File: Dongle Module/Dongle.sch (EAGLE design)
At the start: 74 parts, among them Q2 2.5A/30V, U1 RFM69HCW, U10 74AHC1G125, U2 HALL-EFFECTSMD, U3 HALL-EFFECTSMD, U4 HALL-EFFECTSMD, U5 HALL-EFFECTSMD, U6 BQ27441-G1, U7 BQ24075, U8 ATSAMD21G-A, U9 3.3V, Y1 32.768kHz

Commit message: Worked on the laser and dongle schematics Placed the parts on the laser and dongle boards in their rough locations
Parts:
- removed C10: 1.0uF, SparkFun-Capacitors:1.0UF50V10%(1206)
- removed C11, C9: 10uF, SparkFun-Capacitors:10UF10V10%(0805)
- removed C3, C4, C5, C6: 0.1uF, SparkFun-Capacitors:0.1UF-25V(+80/-20%)(0603)
- removed C7: 1.0uF, SparkFun-Capacitors:1.0UF-16V-10%(0603)
- removed C8: 0.47uF, SparkFun-Capacitors:CAP0603-CAP
- removed D1: BLU, SparkFun-LED:LED-BLUE0603
- removed D2, D6: RED, SparkFun-LED:LED-RED0603
- removed D3: GREEN, SparkFun-LED:LED-GREEN0603
- removed D4: WHT, SparkFun-LED:LED-WHITE0603
- removed D5: BLUE, SparkFun-LED:LED-BLUE0603
- removed JP10: (no value), SparkFun-Connectors:JST_2MM_MALE
- removed JP11: (no value), mike-temp:M021X02_NO_SILK
- removed L1: FB - 30Ohm, SparkFun-Passives:INDUCTOR0603
- removed R11: 0.01, SparkFun-Resistors:RESISTOR1206
- removed R12: 1.1k, SparkFun-Passives:RESISTOR0603-RES
- removed R13, R14: 4.7K, SparkFun-Resistors:4.7KOHM-1/10W-1%(0603)
- removed R15, R2, R3, R4: 180, SparkFun-Resistors:180OHM1/10W1%(0603)
- removed R16: 1K, SparkFun-Resistors:1KOHM-1/10W-1%(0603)
- removed R17, R24: 100k, SparkFun-Resistors:100KOHM-1/10W-1%(0603)
- removed R18, R19, R22, R26: 10K, SparkFun-Resistors:10KOHM-1/10W-1%(0603)0603
- removed R5, R6, R7, R8, R9: 10K, SparkFun-Resistors:10KOHM1/10W1%(0603)0603
- removed S2: (no value), SparkFun-Electromechanical:SWITCH-SPDT-SMD-A
- removed S4: RESET, samd21-temp:SWITCH-MOMENTARY-2SMD-4.6X2.8MM
- removed SJ6: PWR-LED, SparkFun-Passives:JUMPER-PAD-2-NC_BY_TRACENO_SILK
- removed U2, U3, U4, U5: HALL-EFFECTSMD, SparkFun-Sensors:HALL-EFFECTSMD
- removed U6: BQ27441-G1, battery-management-temp:BQ27441-G1
- removed U7: BQ24075, battery-management-temp:BQ24075
- added ANT: (no value), SparkFun-Connectors:M01PTH_2MM
- added U$1: APA102, SAUVE:APA102
- JP22: value CORTEX_DEBUGPTH -> CORTEX_DEBUGSMD; device samd21-temp:CORTEX_DEBUGPTH -> SparkFun-Connectors:CORTEX_DEBUGSMD
- R1: value 180 -> 330; device SparkFun-Resistors:180OHM1/10W1%(0603) -> SparkFun-Resistors:330OHM1/10W1%(0603)
- S1: value SWITCH-MOMENTARY-2SMD-2 -> SWITCH-MOMENTARY-2SMD-4; device SparkFun-Electromechanical:SWITCH-MOMENTARY-2SMD-2 -> SparkFun-Electromechanical:SWITCH-MOMENTARY-2SMD-4
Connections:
- removed net !CE!: R17.1, U7.!CE!
- removed net !CHG!: R15.2, U7.!CHG!
- removed net !PGOOD!: R16.2, U7.!PGOOD!
- removed net 1.8V: C8.1, U6.VDD
- removed net A0: U8.PA02(AIN0/DAC)
- removed net A1: U8.PB08(AIN2/SER4:0/TC4:0)
- removed net A2: U8.PB09(AIN3/SER4:1/TC4:1)
- removed net A3: U8.PA04(AIN4/REFB/SER0:0/TC0:0)
- removed net AREF: U8.PA03(AIN1/REFA)
- removed net BATTERY_IN: C7.1, JP10.+, R11.2, U6.BAT, U6.SRP
- removed net BLU_PWM: R4.1
- removed net BMS_SCL: R14.1, U6.SCL
- removed net BMS_SDA: R13.1, U6.SDA
- removed net D0/RXI: U8.PA11(AIN19/SER0:3+)
- removed net D1/TXO: U8.PA10(AIN18/SER0:2+)
- removed net D10/SS: U8.PA18(SER1:2+)
- removed net D11/MOSI: U8.PA16(I2C/SER1:0+)
- removed net D12/MISO: U8.PA19(SER1:3+)
- removed net D13/SCK: U8.PA17(I2C/SER1:1+)
- removed net D2: U8.PA14(XIN/SER2:2+)
- removed net D3: U8.PA09(I2C/AIN17/SER0:1+)
- removed net D4: U8.PA08(I2C/AIN16/SER0:0+)
- removed net D5: U8.PA15(XOUT/SER2:3+)
- removed net D6: U8.PA20(SER5:2+)
- removed net D7: U8.PA21(SER5:3+)
- removed net D8: U8.PA06(AIN6/SER0:2/TC1:0)
- removed net D9: U8.PA07(AIN7/SER0:3/TC1:1)
- removed net EN1: R18.2, U7.EN1
- removed net EN2: U7.EN2
- removed net GPOUT: R26.1, U6.GPOUT
- removed net GRN_PWM: R2.1
- removed net HALL_DWN: R7.2, U3.OUT
- removed net HALL_LFT: R8.2, U4.OUT
- removed net HALL_RHT: R9.2, U5.OUT
- removed net HALL_UP: R6.2, U2.OUT
- removed net ILIM: R12.1, U7.ILIM
- removed net N$1: D3.A, R2.2
- removed net N$11: D5.C, R15.1
- removed net N$12: D6.C, R16.1
- removed net N$2: D2.A, R3.2
- removed net N$23: D7.C, SJ6.2
- removed net N$3: D1.A, R4.2
- removed net N$4: D4.A, R1.2
- removed net N$5: R24.2, S2.O
- removed net OUT: C9.1, D5.A, D6.A, R13.2, R14.2, R18.1, R19.1, R26.2, U7.OUT
- removed net RED_PWM: R3.1
- removed net RF_NSS: U1.NSS
- removed net RX_LED: U8.PB03(AIN11/SER5:1)
- removed net SCL: U8.PA23(I2C/SER3:0+)
- removed net SDA: U8.PA22(I2C/SER3:0+)
- removed net SYSOFF: S2.P, U7.SYSOFF
- removed net TRK_BTN: R5.2, S1.2
- removed net TS: R22.2, U6.BIN, U7.TS
- removed net TX_LED: U8.PA27
- removed net VCC: C3.1, C4.1, C5.1, C6.1, R5.1, R6.1, R7.1, R8.1, R9.1, U2.VCC, U3.VCC, U4.VCC, U5.VCC
- removed net V_BATT: C11.1, R11.1, R24.1, U6.SRN, U7.BAT
- removed net WHT_PWM: R1.1
- new net APA_CLK: U$1.CKI, U8.PA09(I2C/AIN17/SER0:1+)
- new net APA_MOSI: U$1.SDI, U8.PA08(I2C/AIN16/SER0:0+)
- new net RF_SS: U1.NSS, U8.PA18(SER1:2+)
- new net SEL_BTN: R1.2, S1.1, U8.PA15(XOUT/SER2:3+)
- net !RESET: no longer S4.2
- net 3.3V: now also S1.2, U$1.VCC; no longer L1.1
- net ANT: now also ANT.1
- net GND: now also D7.C, R1.1, U$1.GND; no longer C10.2, C11.2, C3.2, C4.2, C5.2, C6.2, C7.2, C8.2, C9.2, D1.C, D2.C, D3.C, D4.C, JP10.-, JP11.2, R12.2, R17.2, R19.2, R22.1, S1.1, S2.S, S4.1, SJ6.1, U2.GND, U3.GND, U4.GND, U5.GND, U6.PWPD, U6.VSS, U7.EP, U7.TMR, U7.VSS
- net RF_MISO: now also U8.PA19(SER1:3+)
- net RF_MOSI: now also U8.PA16(I2C/SER1:0+)
- net RF_SCK: now also U8.PA17(I2C/SER1:1+)
- net VDDANA: no longer L1.2
- net V_USB: no longer C10.1, JP11.1, U7.IN
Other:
- note removed: "BQ24075 - 1.5A USB-Friendly LiPo Battery Charger & Power-Path Management"
- note removed: "BQ27441-G1 Fuel Gauge"
- note removed: "Battery Charger/Monitor"
- note removed: "Battery Input"
- note removed: "Battery Range: 3.3-4.2V"
- note removed: "Charge Current Select"
- note removed: "I2C ADDR: 0x55"
- note removed: "I2C Pull-Ups"
- note removed: "PA12 is SPI MISO (on SPI header)."
- note removed: "PA13 is DGI GPIO0 (goes to EDBG)."
- note removed: "PA5 is A4"
- note removed: "PB2 is A5"
- note removed: "SYSOFF controls supply to the V_OUT pin. SYSOFF is active-high HIGH=OFF LOW=ON"
- note removed: "Shutoff Switch"
- note removed: "Supply Input"
- note removed: "Supply range: 4.35-6.4V"
- note removed: "TRACKBALL"
- note removed: "VCC Range: 2.5V - 5.25V"
- note removed: "VDD is 1.8V generated internally"
- moved on the sheet: C1, C12, C13, C14, C15, C16, C17, C18, C19, C2, D7, F1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

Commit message: Created, placed, and routed a starter board for the Camera Module
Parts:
- ANT: device SparkFun-Connectors:M01PTH_2MM -> SparkFun-Connectors:M01PTH_NO_SILK_YES_STOP
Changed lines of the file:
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@@
 <part name="GND5" library="SparkFun-Aesthetics" deviceset="GND" device=""/>
 <part name="SUPPLY5" library="SparkFun-Aesthetics" deviceset="3.3V" device=""/>
-<part name="ANT" library="SparkFun-Connectors" deviceset="M01" device="PTH_2MM"/>
+<part name="ANT" library="SparkFun-Connectors" deviceset="M01" device="PTH_NO_SILK_YES_STOP"/>
 </parts>
 <sheets>

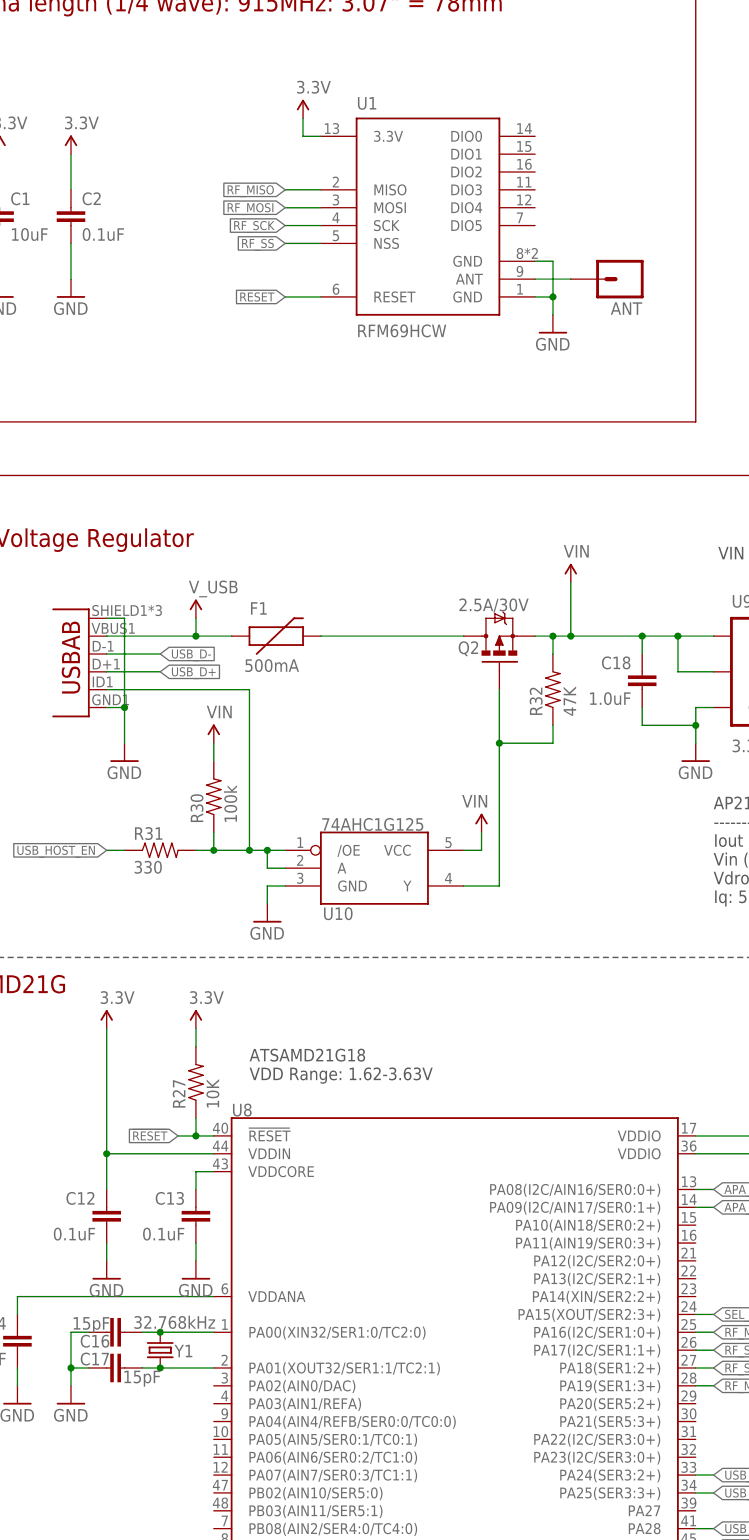
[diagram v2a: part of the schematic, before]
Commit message: Updated the RFM69 library to be closer to C. millis() is the only function hat needs to be updated now.
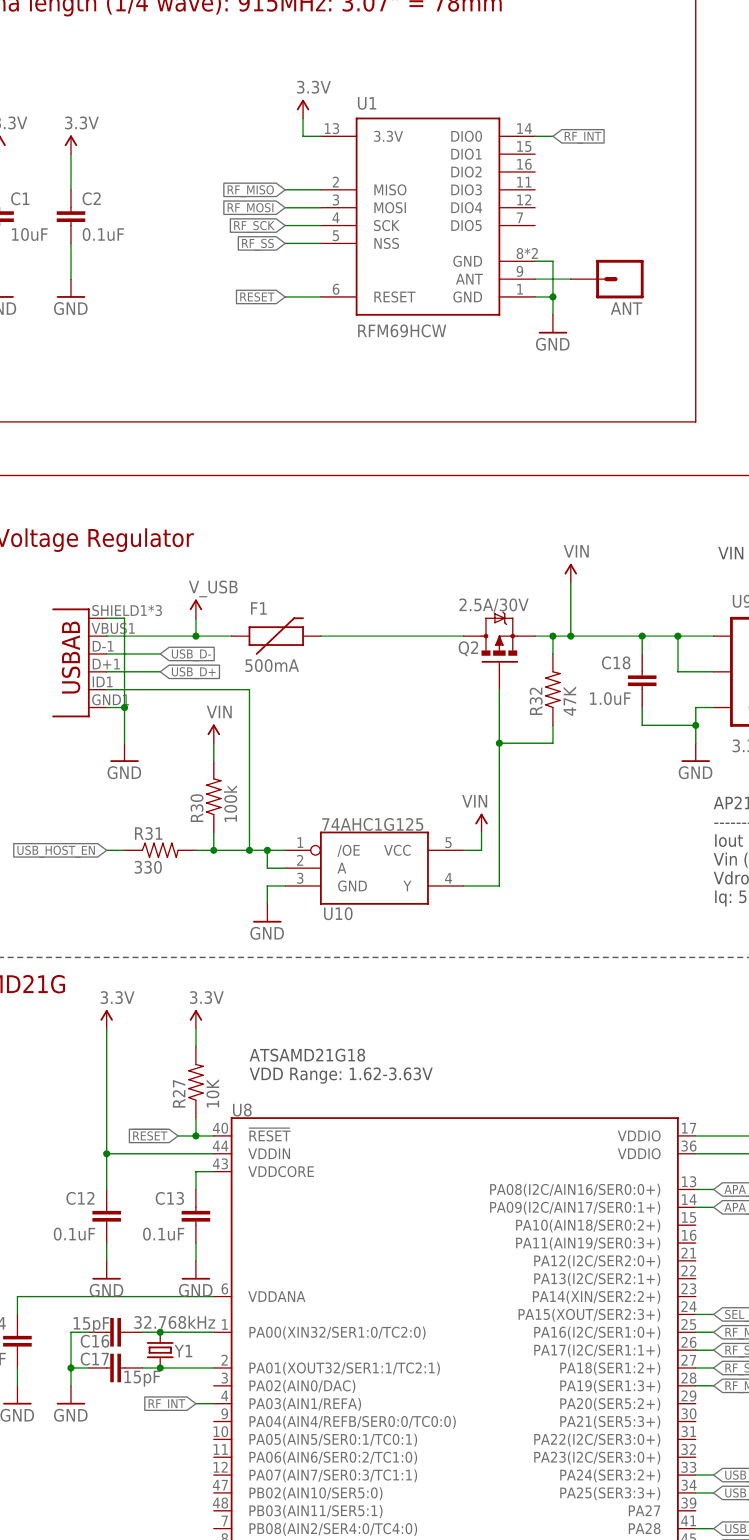
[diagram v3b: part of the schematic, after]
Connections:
- new net RF_INT: U1.DIO0, U8.PA03(AIN1/REFA)
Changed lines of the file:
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@@
+</segment>
+</net>
+<net name="RF_INT" class="0">
+<segment>
+<pinref part="U1" gate="G$1" pin="DIO0"/>
+<wire x1="91.44" y1="228.6" x2="93.98" y2="228.6" width="0.1524" layer="91"/>
+<label x="93.98" y="228.6" size="1.27" layer="95" xref="yes"/>
+</segment>
+<segment>
+<pinref part="U8" gate="G$1" pin="PA03(AIN1/REFA)"/>
+<wire x1="45.72" y1="48.26" x2="43.18" y2="48.26" width="0.1524" layer="91"/>
+<label x="43.18" y="48.26" size="1.27" layer="95" rot="R180" xref="yes"/>
 </segment>
 </net>

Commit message: Finalized all PCBs
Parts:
- C12, C13, C14, C15: device SparkFun-Capacitors:0.1UF-16V(+-10%)(0402) -> SparkFun-Capacitors:CAP0603-CAP
- C16, C17: device samd21-temp:15PF-50V(+-5%)(0402) -> SparkFun-Capacitors:CAP0603-CAP
- D7: value RED -> GREEN
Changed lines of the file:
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@@
 <part name="U8" library="samd21-temp" deviceset="ATSAMD21G" device="-A"/>
 <part name="GND40" library="SparkFun-Aesthetics" deviceset="GND" device=""/>
-<part name="C12" library="SparkFun-Capacitors" deviceset="0.1UF-16V(+-10%)(0402)" device="" value="0.1uF"/>
-<part name="C13" library="SparkFun-Capacitors" deviceset="0.1UF-16V(+-10%)(0402)" device="" value="0.1uF"/>
-<part name="C14" library="SparkFun-Capacitors" deviceset="0.1UF-16V(+-10%)(0402)" device="" value="0.1uF"/>
-<part name="C15" library="SparkFun-Capacitors" deviceset="0.1UF-16V(+-10%)(0402)" device="" value="0.1uF"/>
+<part name="C12" library="SparkFun-Capacitors" deviceset="CAP" device="0603-CAP" value="0.1uF"/>
+<part name="C13" library="SparkFun-Capacitors" deviceset="CAP" device="0603-CAP" value="0.1uF"/>
+<part name="C14" library="SparkFun-Capacitors" deviceset="CAP" device="0603-CAP" value="0.1uF"/>
+<part name="C15" library="SparkFun-Capacitors" deviceset="CAP" device="0603-CAP" value="0.1uF"/>
 <part name="R27" library="SparkFun-Resistors" deviceset="10KOHM-1/10W-1%(0603)" device="0603" value="10K"/>
 <part name="SUPPLY12" library="SparkFun-Aesthetics" deviceset="3.3V" device=""/>
@@
 <part name="GND42" library="SparkFun-Aesthetics" deviceset="GND" device=""/>
 <part name="GND43" library="SparkFun-Aesthetics" deviceset="GND" device=""/>
-<part name="C16" library="samd21-temp" deviceset="15PF-50V(+-5%)(0402)" device="" value="15pF"/>
-<part name="C17" library="samd21-temp" deviceset="15PF-50V(+-5%)(0402)" device="" value="15pF"/>
+<part name="C16" library="SparkFun-Capacitors" deviceset="CAP" device="0603-CAP" value="15pF"/>
+<part name="C17" library="SparkFun-Capacitors" deviceset="CAP" device="0603-CAP" value="15pF"/>
 <part name="GND44" library="SparkFun-Aesthetics" deviceset="GND" device=""/>
 <part name="SUPPLY15" library="SparkFun-Aesthetics" deviceset="3.3V" device=""/>
@@
 <part name="GND49" library="SparkFun-Aesthetics" deviceset="GND" device=""/>
 <part name="SUPPLY16" library="SparkFun-Aesthetics" deviceset="3.3V" device=""/>
-<part name="D7" library="SparkFun-LED" deviceset="LED-RED" device="0603" value="RED"/>
+<part name="D7" library="SparkFun-LED" deviceset="LED-RED" device="0603" value="GREEN"/>
 <part name="R28" library="SparkFun-Resistors" deviceset="330OHM1/10W1%(0603)" device="" value="330"/>
 <part name="SUPPLY17" library="SparkFun-Aesthetics" deviceset="3.3V" device=""/>
@@
 <wire x1="0" y1="0" x2="0" y2="180.34" width="0.1524" layer="94"/>
 <text x="165.1" y="38.1" size="5.08" layer="94" ratio="15">SAMD21G18</text>
+<wire x1="132.08" y1="256.54" x2="208.28" y2="256.54" width="0.1524" layer="94"/>
+<wire x1="208.28" y1="256.54" x2="208.28" y2="190.5" width="0.1524" layer="94"/>
+<wire x1="208.28" y1="190.5" x2="132.08" y2="190.5" width="0.1524" layer="94"/>
+<wire x1="132.08" y1="190.5" x2="132.08" y2="256.54" width="0.1524" layer="94"/>
 </plain>
 <instances>
@@
 <instance part="C16" gate="G$1" x="33.02" y="58.42" smashed="yes" rot="R90">
 <attribute name="NAME" x="30.988" y="58.039" size="1.778" layer="95" rot="R180"/>
-<attribute name="VALUE" x="30.988" y="58.801" size="1.778" layer="96" rot="MR0"/>
 </instance>
 <instance part="C17" gate="G$1" x="30.48" y="53.34" smashed="yes" rot="R270">
 <attribute name="NAME" x="30.988" y="53.721" size="1.778" layer="95" rot="MR0"/>
-<attribute name="VALUE" x="32.766" y="52.959" size="1.778" layer="96" rot="MR180"/>
 </instance>
 <instance part="GND44" gate="1" x="25.4" y="48.26"/>
@@
 <instance part="SUPPLY24" gate="G$1" x="96.52" y="165.1"/>
 <instance part="SUPPLY18" gate="G$1" x="43.18" y="160.02"/>
-<instance part="S1" gate="G$1" x="172.72" y="241.3"/>
+<instance part="S1" gate="G$1" x="172.72" y="241.3" smashed="yes">
+<attribute name="NAME" x="170.18" y="243.84" size="1.778" layer="95"/>
+</instance>
 <instance part="SUPPLY3" gate="G$1" x="182.88" y="246.38"/>
 <instance part="GND4" gate="1" x="162.56" y="223.52"/>

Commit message: push ui.c again
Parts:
- C12, C13, C14, C15: device SparkFun-Capacitors:CAP0603-CAP -> SparkFun-Capacitors:0.1UF-16V(+-10%)(0402)
- C16, C17: device SparkFun-Capacitors:CAP0603-CAP -> samd21-temp:15PF-50V(+-5%)(0402)
- D7: value GREEN -> RED
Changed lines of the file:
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@@
 <part name="U8" library="samd21-temp" deviceset="ATSAMD21G" device="-A"/>
 <part name="GND40" library="SparkFun-Aesthetics" deviceset="GND" device=""/>
-<part name="C12" library="SparkFun-Capacitors" deviceset="CAP" device="0603-CAP" value="0.1uF"/>
-<part name="C13" library="SparkFun-Capacitors" deviceset="CAP" device="0603-CAP" value="0.1uF"/>
-<part name="C14" library="SparkFun-Capacitors" deviceset="CAP" device="0603-CAP" value="0.1uF"/>
-<part name="C15" library="SparkFun-Capacitors" deviceset="CAP" device="0603-CAP" value="0.1uF"/>
+<part name="C12" library="SparkFun-Capacitors" deviceset="0.1UF-16V(+-10%)(0402)" device="" value="0.1uF"/>
+<part name="C13" library="SparkFun-Capacitors" deviceset="0.1UF-16V(+-10%)(0402)" device="" value="0.1uF"/>
+<part name="C14" library="SparkFun-Capacitors" deviceset="0.1UF-16V(+-10%)(0402)" device="" value="0.1uF"/>
+<part name="C15" library="SparkFun-Capacitors" deviceset="0.1UF-16V(+-10%)(0402)" device="" value="0.1uF"/>
 <part name="R27" library="SparkFun-Resistors" deviceset="10KOHM-1/10W-1%(0603)" device="0603" value="10K"/>
 <part name="SUPPLY12" library="SparkFun-Aesthetics" deviceset="3.3V" device=""/>
@@
 <part name="GND42" library="SparkFun-Aesthetics" deviceset="GND" device=""/>
 <part name="GND43" library="SparkFun-Aesthetics" deviceset="GND" device=""/>
-<part name="C16" library="SparkFun-Capacitors" deviceset="CAP" device="0603-CAP" value="15pF"/>
-<part name="C17" library="SparkFun-Capacitors" deviceset="CAP" device="0603-CAP" value="15pF"/>
+<part name="C16" library="samd21-temp" deviceset="15PF-50V(+-5%)(0402)" device="" value="15pF"/>
+<part name="C17" library="samd21-temp" deviceset="15PF-50V(+-5%)(0402)" device="" value="15pF"/>
 <part name="GND44" library="SparkFun-Aesthetics" deviceset="GND" device=""/>
 <part name="SUPPLY15" library="SparkFun-Aesthetics" deviceset="3.3V" device=""/>
@@
 <part name="GND49" library="SparkFun-Aesthetics" deviceset="GND" device=""/>
 <part name="SUPPLY16" library="SparkFun-Aesthetics" deviceset="3.3V" device=""/>
-<part name="D7" library="SparkFun-LED" deviceset="LED-RED" device="0603" value="GREEN"/>
+<part name="D7" library="SparkFun-LED" deviceset="LED-RED" device="0603" value="RED"/>
 <part name="R28" library="SparkFun-Resistors" deviceset="330OHM1/10W1%(0603)" device="" value="330"/>
 <part name="SUPPLY17" library="SparkFun-Aesthetics" deviceset="3.3V" device=""/>
@@
 <wire x1="0" y1="0" x2="0" y2="180.34" width="0.1524" layer="94"/>
 <text x="165.1" y="38.1" size="5.08" layer="94" ratio="15">SAMD21G18</text>
-<wire x1="132.08" y1="256.54" x2="208.28" y2="256.54" width="0.1524" layer="94"/>
-<wire x1="208.28" y1="256.54" x2="208.28" y2="190.5" width="0.1524" layer="94"/>
-<wire x1="208.28" y1="190.5" x2="132.08" y2="190.5" width="0.1524" layer="94"/>
-<wire x1="132.08" y1="190.5" x2="132.08" y2="256.54" width="0.1524" layer="94"/>
 </plain>
 <instances>
@@
 <instance part="C16" gate="G$1" x="33.02" y="58.42" smashed="yes" rot="R90">
 <attribute name="NAME" x="30.988" y="58.039" size="1.778" layer="95" rot="R180"/>
+<attribute name="VALUE" x="30.988" y="58.801" size="1.778" layer="96" rot="MR0"/>
 </instance>
 <instance part="C17" gate="G$1" x="30.48" y="53.34" smashed="yes" rot="R270">
 <attribute name="NAME" x="30.988" y="53.721" size="1.778" layer="95" rot="MR0"/>
+<attribute name="VALUE" x="32.766" y="52.959" size="1.778" layer="96" rot="MR180"/>
 </instance>
 <instance part="GND44" gate="1" x="25.4" y="48.26"/>
@@
 <instance part="SUPPLY24" gate="G$1" x="96.52" y="165.1"/>
 <instance part="SUPPLY18" gate="G$1" x="43.18" y="160.02"/>
-<instance part="S1" gate="G$1" x="172.72" y="241.3" smashed="yes">
-<attribute name="NAME" x="170.18" y="243.84" size="1.778" layer="95"/>
-</instance>
+<instance part="S1" gate="G$1" x="172.72" y="241.3"/>
 <instance part="SUPPLY3" gate="G$1" x="182.88" y="246.38"/>
 <instance part="GND4" gate="1" x="162.56" y="223.52"/>
